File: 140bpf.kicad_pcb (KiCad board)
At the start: 2 copper layers, 41.9 x 12.7 mm, 3 parts, among them J1 Conn_Coaxial, J2 Conn_Coaxial, U1 RBP-140+

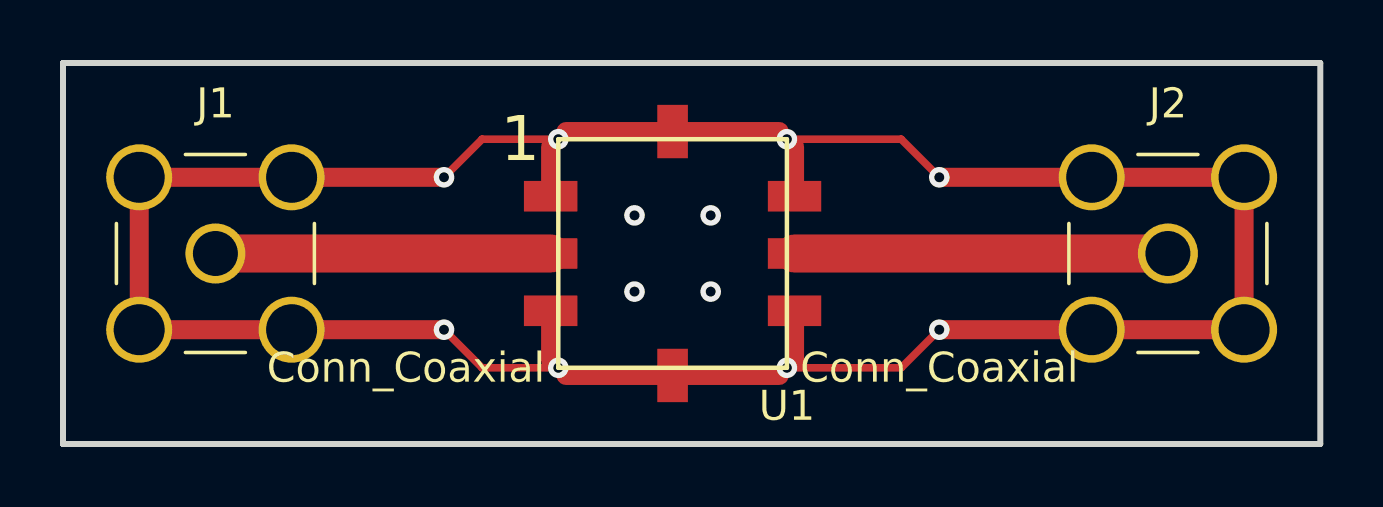
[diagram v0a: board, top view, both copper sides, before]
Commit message: Fixup silkscreen issues
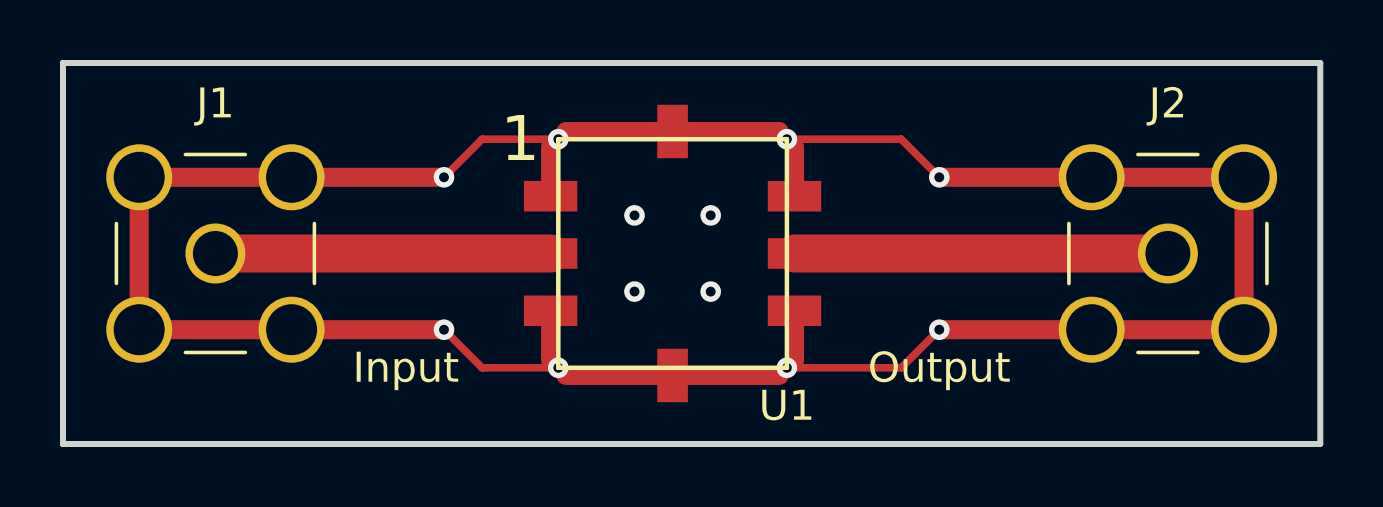
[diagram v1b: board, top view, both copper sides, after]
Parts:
- J1: value Conn_Coaxial -> Input
- J2: value Conn_Coaxial -> Output
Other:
- net class Default removed
